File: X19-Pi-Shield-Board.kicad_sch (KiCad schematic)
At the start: 49 parts, among them IC1 STM32C542CCT6, J1 Raspberry_Pi_4, J2 Conn_01x02, J3 Conn_01x02, J4 Conn_01x04, J5 Conn_01x04, J6 Conn_01x03, J7 Conn_01x03, J8 Conn_02x05_Odd_Even, SW1 SW_Push, U1 MIC5504-3.3YM5, U2 BME280, U3 INA237AIDGSR, U4 TCAN1044VDRQ1, U5 MCP2518FDT-E/QBB, U6 TCAN1044VDRQ1, Y1 ECS-120-18-33-JGN-TR, Y2 ECS-120-18-33-JGN-TR

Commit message: final...
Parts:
- removed C7, C8: 22p, symbol Device:C
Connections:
- net I2C SCL: no longer J1.28 (ID_SC_I2C0/GPIO01)
- net I2C SDA: no longer J1.27 (ID_SD_I2C0/GPIO00)

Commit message: Pre Sch Review - Nick Changes
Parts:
- removed C1, C2: 1uF, Package_SO:SOIC-8_3.9x4.9mm_P1.27mm, symbol Device:C
- removed C11, C6: 0.1u, symbol Device:C
- removed C12, C13, C3, C4: 27pF, symbol Device:C
- removed C14, C16, C17, C18: 100n, symbol Device:C
- removed C15: 2.2u, symbol Device:C
- removed C19: 4.7u, symbol Device:C
- removed C5: 0.1uF, symbol Device:C
- removed IC1: STM32C542CCT6, QFP50P900X900X160-48N, symbol STM32C542CCT6:STM32C542CCT6
- removed J8: Conn_02x05_Odd_Even, Oscillator:Oscillator_SMD_ECS_2520MV-xxx-xx-4Pin_2.5x2.0mm, symbol Connector_Generic:Conn_02x05_Odd_Even
- removed R1: 1m, D0008A-IPC_A, symbol Device:R_Small_US
- removed R2, R3, R4: 4.7k, symbol Device:R_Small_US
- removed R5: 10k, Resistor_THT:R_Array_SIP4, symbol Device:R_US
- removed SW1: SW_Push, Button_Switch_THT:SW_NKK_GW12LJP, symbol Switch:SW_Push
- removed U1: MIC5504-3.3YM5, Package_TO_SOT_SMD:SOT-23-5, symbol Regulator_Linear:MIC5504-3.3YM5
- removed U3: INA237AIDGSR, VSSOP_IDGSR_TEX, symbol INA237AIDGSR:INA237AIDGSR
- removed U4, U6: TCAN1044VDRQ1, D0008A-IPC_A, symbol TCAN1044VDRQ1:TCAN1044VDRQ1
- removed U5: MCP2518FDT-E/QBB, VDFN14_QBB_MCH, symbol MCP2518FDT_E_QBB:MCP2518FDT-E_QBB
- removed Y1, Y2: ECS-120-18-33-JGN-TR, ECS-120-18-33-JGN-TR:XTAL_ECS-120-18-33-JGN-TR, symbol ECS-120-18-33-JGN-TR:ECS-120-18-33-JGN-TR
- added CR2: ESD2CAN24DBZRQ1, SOT-23_DBZ_TEX, symbol board_control_manual_lib:ESD2CAN24DBZRQ1
- added D1, D2, D3, D4: LED, symbol Device:LED
- added H4: MountingHole_Pad, symbol Mechanical:MountingHole_Pad
- added JP1: Jumper_2_Open, symbol Jumper:Jumper_2_Open
- added R10: 10K, symbol Device:R_US
- added R6, R8: 2.2K, symbol Device:R_US
- added R7, R9: 1K, symbol Device:R_US
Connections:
- net CS_STM is gone; now on net +3.3V: U2.2 (CSB)
- net MOSI_STM is gone; now on net I2C_SDA_STM: U2.3 (SDI)
- net SCLK_STM is gone; now on net I2C_SCL_STM: U2.4 (SCK)
- net +3.3V: now also C10.2, TP3.1, U2.8 (VDD), D2.2 (A), JP1.2 (B)
- net +5V: now also TP2.1, D1.2 (A); no longer C10.2, U2.8 (VDD)
- net +5V_UNFILT: now also TP1.1
- net CAN+: now also CR2.2
- net CAN-: now also CR2.1
- net GND: now also TP4.1, CR2.3, R10.2, R6.2, R7.2, R8.2, R9.2
- net PI_LED: now reaches J1.31 (GPCLK2/GPIO06)
- net PI_LED: now also D3.2 (A)
- net 3.3VLDO: no longer names the net of J1.1 (3V3), J1.17 (3V3)
- net CS renamed CS_PI
- net I2C SCL renamed I2C_SCL_STM
- net I2C SDA renamed I2C_SDA_STM
- net MISO renamed MISO_PI
- net MISO_STM: no longer names the net of U2.5 (SDO)
- net MISO_STM: now also JP1.1 (A), R10.1
- net MOSI renamed MOSI_PI
- net SCLK renamed SCLK_PI
- net STBY renamed STBY_MCP
- new net: D2.1 (K), R7.1
- new net: D4.1 (K), R9.1
- new net: D1.1 (K), R6.1
- new net: D3.1 (K), R8.1
- new net STM_LED: D4.2 (A)
- no-connect marks 49 -> 22
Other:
- added sheet CAN (can.kicad_sch)
- added sheet MCU (mcu.kicad_sch)
- added sheet Power (power.kicad_sch)
- note added: "CSB->VDDIO = I2C"
- note added: "I2C Address: 0x76 (SDO GND) 0x77 (SDO Vddio)"
- note added: "TVS Close to CAN connector"
- note added: "~10mA thru LED"
- note removed: "C16 C17 C18 all for VDD_1 2 3. 4.7u parallel with all three VDD cap to ground C14 to VREF+ C15 to VCap"
- moved on the sheet: C10, C9, H1, H2, H3, J1, J2, J3, J4, J5, J6, J7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

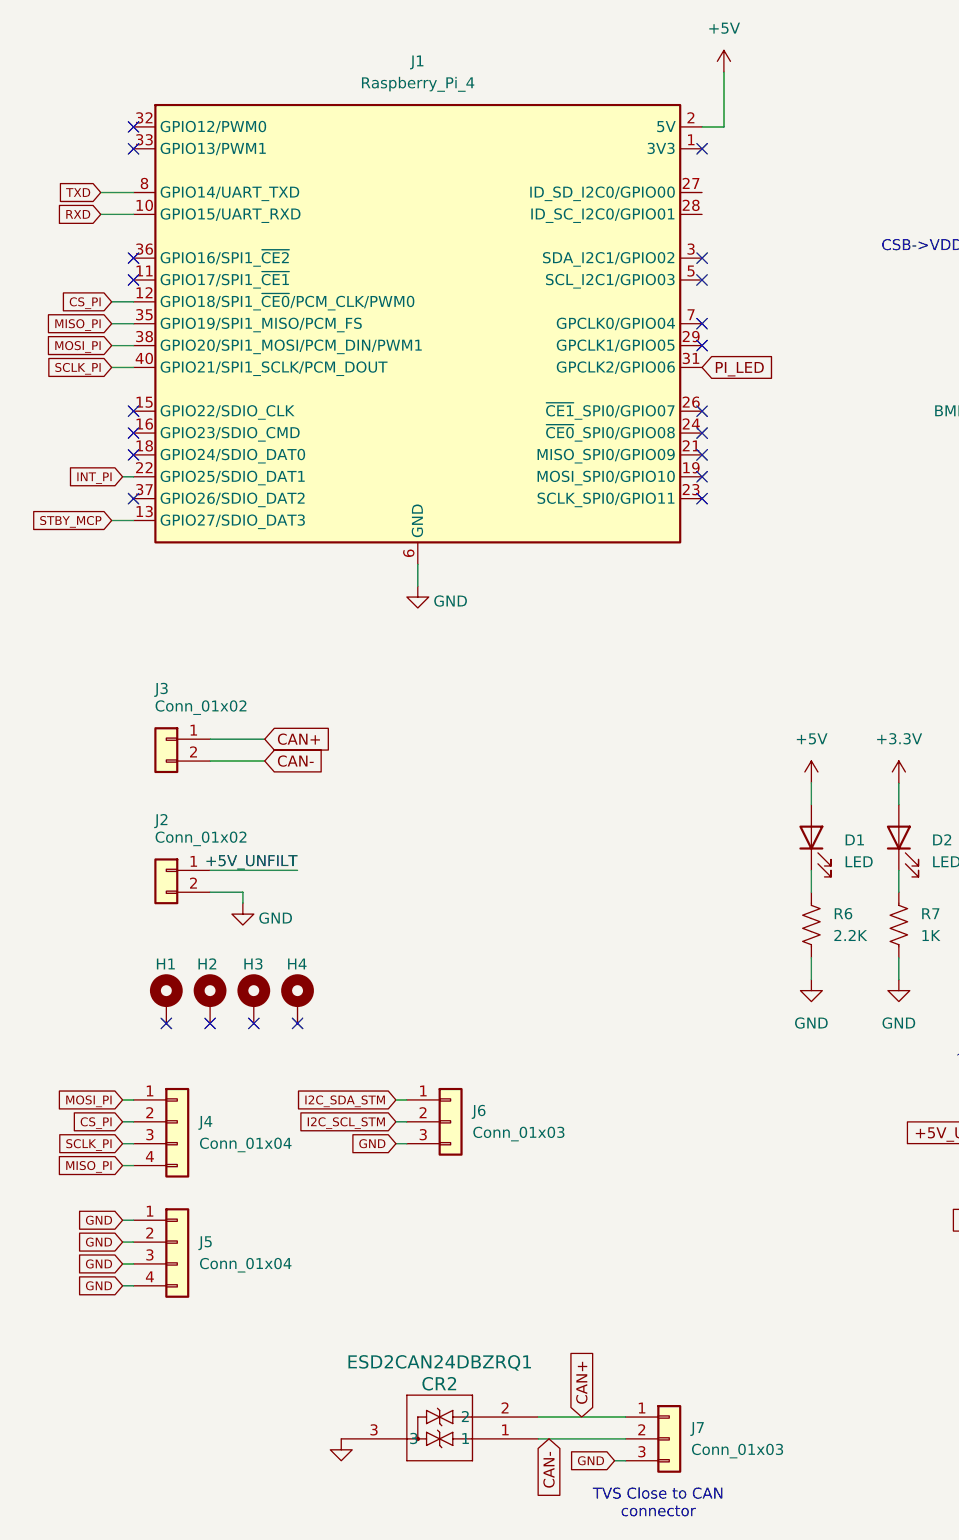
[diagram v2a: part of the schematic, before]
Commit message: adding back can net class and removing extra conns
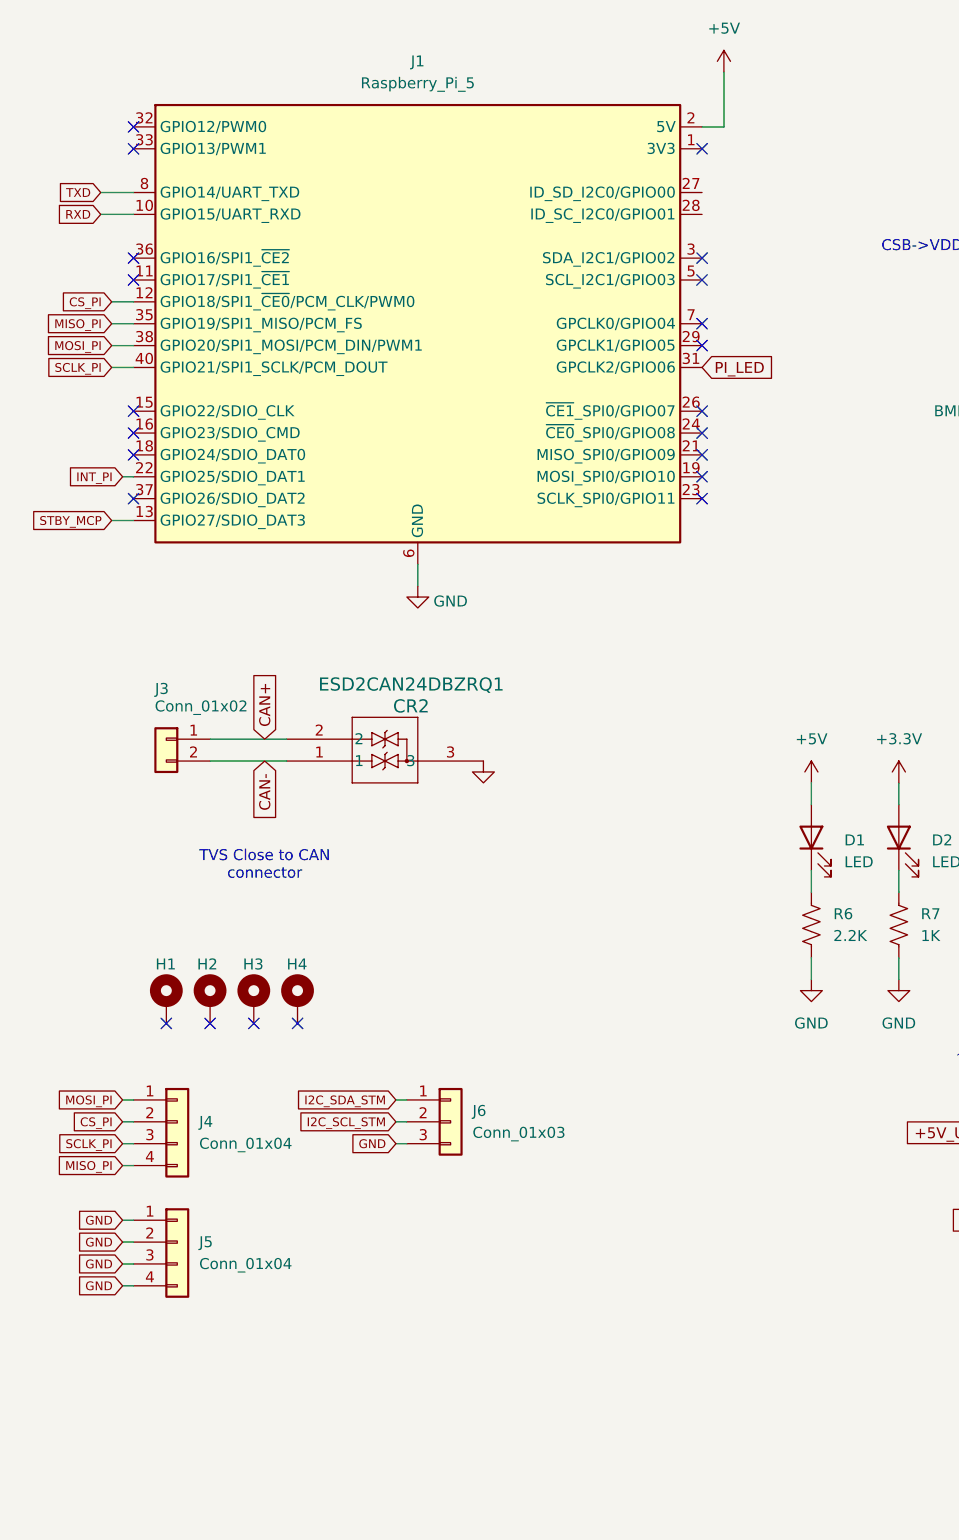
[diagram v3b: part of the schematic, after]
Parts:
- removed J2: Conn_01x02, rov_connectors:0436500200, symbol Connector_Generic:Conn_01x02
- removed J7: Conn_01x03, Oscillator:Oscillator_SMD_ECS_2520MV-xxx-xx-4Pin_2.5x2.0mm, symbol Connector_Generic:Conn_01x03
- J1: value Raspberry_Pi_4 -> Raspberry_Pi_5

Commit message: In progress, changed stdby
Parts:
- removed J4: Conn_01x04, Oscillator:Oscillator_SMD_ECS_2520MV-xxx-xx-4Pin_2.5x2.0mm, symbol Connector_Generic:Conn_01x04
- added J7: Conn_01x05_Pin, symbol Connector:Conn_01x05_Pin
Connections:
- net CS_PI: now also J7.3 (Pin_3)
- net GND: now also J7.5 (Pin_5)
- net MISO_PI: now also J7.1 (Pin_1)
- net MOSI_PI: now also J7.4 (Pin_4)
- net SCLK_PI: now also J7.2 (Pin_2)
- net +5V_UNFILT renamed +5V_RAW
- net STBY_MCP: no longer names the net of J1.13 (GPIO27/SDIO_DAT3)
- no-connect marks 22 -> 23

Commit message: Relatively final changes
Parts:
- added C19: 470u, symbol Device:C
- added C26: 10u, symbol Device:C
- added C27: 100n, symbol Device:C
- added J4: Conn_01x06, symbol Connector_Generic:Conn_01x06
- added TP6, TP7: TestPoint, symbol Connector:TestPoint
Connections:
- net +3.3V: now also J4.1 (Pin_1)
- net CAN+: now also TP6.1
- net CAN-: now also TP7.1
- net CS_PI: now also J4.5 (Pin_5)
- net GND: now also C19.2, C26.2, C27.2, J4.6 (Pin_6)
- net +5V renamed +5.1V
- net +5.1V: now also C19.1, C26.1, C27.1
- net +5V_RAW renamed +5.1V_RAW
- new net MISO: J4.3 (Pin_3)
- new net MOSI: J4.4 (Pin_4)
- new net SCLK: J4.2 (Pin_2)
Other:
- note added: "Backup SPI"
- note added: "I2C Address: 0x76 (SDO GND) (DEFAULT) 0x77 (SDO Vddio) Address Select Below"
- note removed: "I2C Address: 0x76 (SDO GND) 0x77 (SDO Vddio)"
- moved on the sheet: CR2, J3

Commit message: Some minor changes
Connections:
- net CS_STM: now reaches J1.11 (GPIO17/SPI1_~{CE1})
- no-connect marks 23 -> 22
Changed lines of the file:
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@@
-	)
-	(no_connect
-		(at 29.21 48.26)
 	)
 	(no_connect
@@
 	(wire
 		(pts
+			(xy 26.67 48.26) (xy 29.21 48.26)
+		)
+		(stroke
+			(width 0)
+			(type default)
+		)
+	)
+	(wire
+		(pts
 			(xy 59.69 143.51) (xy 60.96 143.51)
 		)
@@
 			)
 		)
+	)
+	(global_label "CS_STM"
+		(shape input)
+		(at 26.67 48.26 180)
+		(fields_autoplaced yes)
+		(effects
+			(font
+				(size 1.27 1.27)
+			)
+			(justify right)
+		)
+		(property "Intersheetrefs" "${INTERSHEET_REFS}"
+			(at 17.2634 48.26 0)
+			(hide yes)
+			(show_name no)
+			(do_not_autoplace no)
+			(effects
+				(font
+					(size 1.27 1.27)
+				)
+				(justify right)
+			)
+		)

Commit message: updated footprints
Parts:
- CR2: footprint SOT-23_DBZ_TEX -> (none)
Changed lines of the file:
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@@
 			)
 		)
-		(property "Footprint" "SOT-23_DBZ_TEX"
+		(property "Footprint" ""
 			(at 34.036 110.236 0)
 			(hide yes)

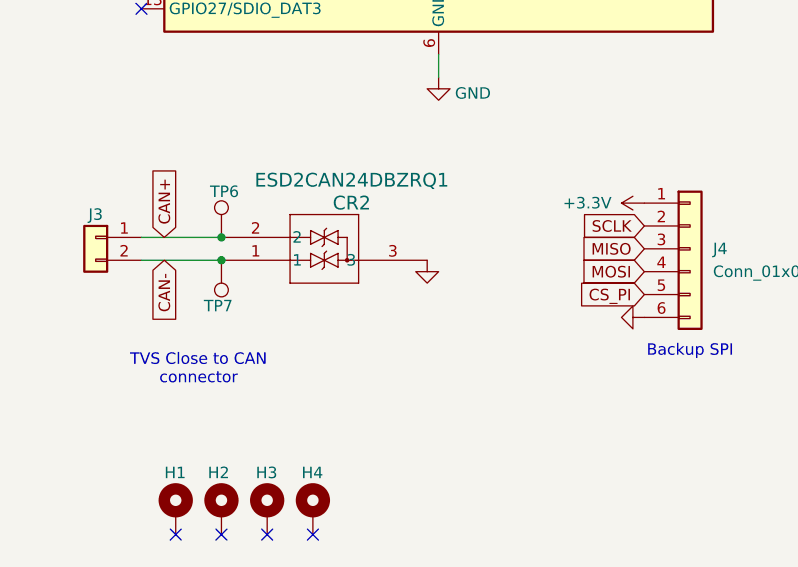
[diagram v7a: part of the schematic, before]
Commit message: added footprints
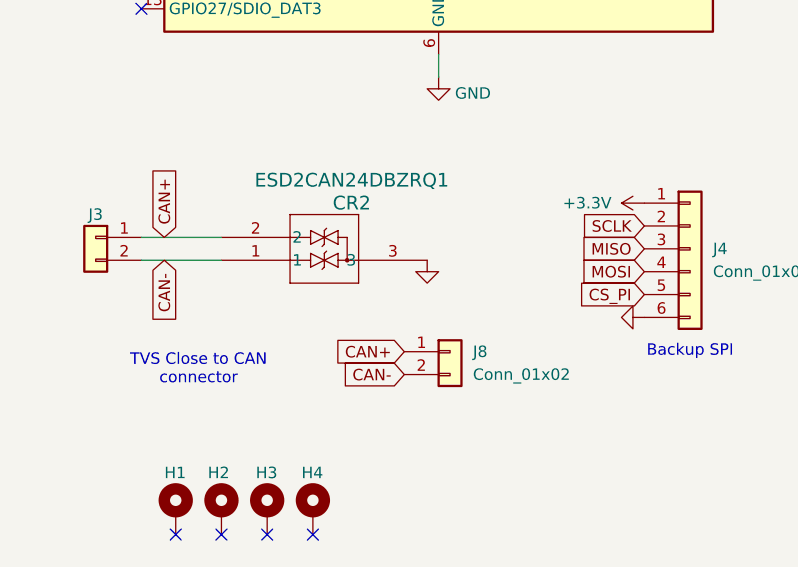
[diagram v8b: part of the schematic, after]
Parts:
- removed TP6, TP7: TestPoint, symbol Connector:TestPoint
- added J8: Conn_01x02, Package_DFN_QFN:DFN-14-1EP_3x4.5mm_P0.65mm_EP1.65x4.25mm, symbol Connector_Generic:Conn_01x02
- C10, C19, C26, C27, C9: footprint (none) -> Capacitor_SMD:C_0603_1608Metric_Pad1.08x0.95mm_HandSolder
- D1, D2, D3, D4: footprint (none) -> LED_SMD:LED_0603_1608Metric_Pad1.05x0.95mm_HandSolder
- H1, H2, H3, H4: footprint (none) -> MountingHole:MountingHole_3.2mm_M3
- J1: footprint Connector_PinSocket_2.54mm:PinSocket_2x20_P2.54mm_Vertical -> Connector_PinHeader_2.54mm:PinHeader_2x20_P2.54mm_Vertical
- J4: footprint (none) -> Connector_PinHeader_2.54mm:PinHeader_1x06_P2.54mm_Horizontal
- J7: footprint (none) -> Connector_PinHeader_2.54mm:PinHeader_1x05_P2.54mm_Horizontal
- JP1: footprint (none) -> Connector_PinHeader_2.54mm:PinHeader_1x02_P2.54mm_Vertical
- R10, R6, R7, R8, R9: footprint (none) -> Resistor_SMD:R_0603_1608Metric_Pad0.98x0.95mm_HandSolder
- TP1, TP2, TP3, TP4: footprint (none) -> TestPoint:TestPoint_Pad_D2.5mm
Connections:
- net CAN+: now also J8.1 (Pin_1)
- net CAN-: now also J8.2 (Pin_2)
